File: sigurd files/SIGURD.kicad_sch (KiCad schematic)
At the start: 79 parts, among them J1 jst_sh 4, J10 CAN out (optional), J11 12V/24V Terminal, J2 Hall sensor, J3 12V Terminal, J4 PWM, J5 24V Terminal, J6 Step Up Terminal, J7 Motor Terminal, J8 INPUT, J9 CAN input, Q1 MMBT3904, U1 LMR50410Y5FQDBVRQ1, U2 STM32U575CGTx, U6 AMS1117-3.3, U8 TCAN334GDCN, Y1 48MHz

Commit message: funny fortnite
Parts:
- added D11: LED, LED_SMD:LED_0603_1608Metric_Pad1.05x0.95mm_HandSolder, symbol Device:LED
- added JP3: SolderJumper_2_Open, Jumper:SolderJumper-2_P1.3mm_Open_TrianglePad1.0x1.5mm, symbol Jumper:SolderJumper_2_Open
- added R31: 1k, Resistor_SMD:R_0603_1608Metric_Pad0.98x0.95mm_HandSolder, symbol Device:R_Small
- added R34: 120, Resistor_SMD:R_0603_1608Metric_Pad0.98x0.95mm_HandSolder, symbol Device:R_Small
- R10, R11, R12, R4, R6, R7: footprint Resistor_SMD:R_0201_0603Metric_Pad0.64x0.40mm_HandSolder -> Resistor_SMD:R_0603_1608Metric_Pad0.98x0.95mm_HandSolder
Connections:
- net +3V3: now also R31.1
- net CAN_H: now also R34.1
- net CAN_L: now also JP3.1 (A)
- net Earth: now also D11.1 (K)
- net VCC: now also J6.3 (Pin_3); no longer J6.2 (Pin_2)
- net at F2.2: now also J6.2 (Pin_2); no longer J6.3 (Pin_3)
- new net: JP3.2 (B), R34.2
- new net: D11.2 (A), R31.2
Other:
- note added: "naming"
- moved on the sheet: C1, C15, C16, C17, C18, C19, C2, C9, F1, FB1, L1, R20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

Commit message: big chungus wholesome 100
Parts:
- removed JP1: SolderJumper_2_Open, Jumper:SolderJumper-2_P1.3mm_Open_TrianglePad1.0x1.5mm, symbol Jumper:SolderJumper_2_Open
- removed R19: 120, Resistor_SMD:R_0603_1608Metric_Pad0.98x0.95mm_HandSolder, symbol Device:R_Small
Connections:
- net pull_1: now also J2.1 (Pin_1), R10.1, R35.2; no longer J2.3 (Pin_3), R37.2, R4.1
- net pull_3: now also J2.3 (Pin_3), R37.2, R4.1; no longer J2.1 (Pin_1), R10.1, R35.2
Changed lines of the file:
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@@
 	(wire
 		(pts
-			(xy 375.92 133.35) (xy 375.92 125.73)
-		)
-		(stroke
-			(width 0)
-			(type default)
-			(color 47 31 255 1)
-		)
-	)
-	(wire
-		(pts
 			(xy 120.65 165.1) (xy 125.73 165.1)
 		)
@@
 	(wire
 		(pts
-			(xy 375.92 116.84) (xy 375.92 118.11)
-		)
-		(stroke
-			(width 0)
-			(type default)
-		)
-	)
-	(wire
-		(pts
 			(xy 97.79 64.77) (xy 97.79 63.5)
 		)
@@
 	(wire
 		(pts
-			(xy 375.92 111.76) (xy 375.92 104.14)
-		)
-		(stroke
-			(width 0)
-			(type default)
-			(color 255 3 242 1)
-		)
-	)
-	(wire
-		(pts
 			(xy 116.84 251.46) (xy 116.84 248.92)
 		)
@@
 		)
 	)
-	(label "pull_1"
-		(at 46.99 119.38 270)
-		(fields_autoplaced yes)
-		(effects
-			(font
-				(size 1.27 1.27)
-			)
-			(justify right bottom)
-		)
-	)
 	(label "SOL3"
 		(at 226.06 144.78 180)
@@
 	)
 	(label "pull_3"
-		(at 74.93 106.68 270)
+		(at 55.88 106.68 270)
 		(fields_autoplaced yes)
 		(effects
@@
 		)
 	)
-	(label "pull_3"
-		(at 81.28 118.11 270)
-		(fields_autoplaced yes)
-		(effects
-			(font
-				(size 1.27 1.27)
-			)
-			(justify right bottom)
-		)
-	)
 	(label "LED_RX"
 		(at 168.91 160.02 0)
@@
 		)
 	)
-	(label "SOL2_OUT"
-		(at 331.47 179.07 180)
+	(label "pull_1"
+		(at 74.93 106.68 270)
 		(fields_autoplaced yes)
 		(effects
@@
 		)
 	)
-	(label "pull_1"
-		(at 55.88 106.68 270)
+	(label "SOL2_OUT"
+		(at 331.47 179.07 180)
 		(fields_autoplaced yes)
 		(effects
@@
 		)
 	)
+	(label "pull_1"
+		(at 81.28 118.11 270)
+		(fields_autoplaced yes)
+		(effects
+			(font
+				(size 1.27 1.27)
+			)
+			(justify right bottom)
+		)
+	)
 	(label "LED_RX"
 		(at 91.44 46.99 0)
@@
 		)
 	)
+	(label "pull_3"
+		(at 46.99 119.38 270)
+		(fields_autoplaced yes)
+		(effects
+			(font
+				(size 1.27 1.27)
+			)
+			(justify right bottom)
+		)
+	)
 	(label "HALL1_buff"
 		(at 226.06 127 180)
@@
 		)
 	)
-	(label "CAN_H"
-		(at 375.92 104.14 0)
-		(fields_autoplaced yes)
-		(effects
-			(font
-				(size 1.27 1.27)
-				(color 255 3 242 1)
-			)
-			(justify left bottom)
-		)
-	)
 	(label "SOL3_SENSE"
 		(at 330.2 200.66 180)
@@
 		)
 	)
-	(label "CAN_L"
-		(at 375.92 133.35 0)
-		(fields_autoplaced yes)
-		(effects
-			(font
-				(size 1.27 1.27)
-				(color 47 31 255 1)
-			)
-			(justify left bottom)
-		)
-	)
 	(label "SOL2"
 		(at 226.06 142.24 180)
@@
 	)
 	(symbol
-		(lib_id "Device:R_Small")
-		(at 375.92 114.3 0)
-		(unit 1)
-		(exclude_from_sim no)
-		(in_bom yes)
-		(on_board yes)
-		(dnp no)
-		(property "Reference" "R19"
-			(at 372.364 115.316 0)
-			(effects
-				(font
-					(size 1.27 1.27)
-				)
-			)
-		)
-		(property "Value" "120"
-			(at 372.364 113.284 0)
-			(effects
-				(font
-					(size 1.27 1.27)
-				)
-			)
-		)
-		(property "Footprint" "Resistor_SMD:R_0603_1608Metric_Pad0.98x0.95mm_HandSolder"
-			(at 375.92 114.3 0)
-			(effects
-				(font
-					(size 1.27 1.27)
-				)
-				(hide yes)
-			)
-		)
-		(property "Datasheet" "~"
-			(at 375.92 114.3 0)
-			(effects
-				(font
-					(size 1.27 1.27)
-				)
-				(hide yes)
-			)
-		)
-		(property "Description" ""
-			(at 375.92 114.3 0)
-			(effects
-				(font
-					(size 1.27 1.27)
-				)
-				(hide yes)
-			)
-		)
-		(pin "1"
-		)
-		(pin "2"
-		)
-		(instances
-			(project "SIGURD"
-				(path "/a4a592a3-08d1-41ec-9dda-18a75407e2f6"
-					(reference "R19")
-					(unit 1)
-				)
-			)
-		)
-	)
-	(symbol
 		(lib_id "1N4448:1N4448")
 		(at 48.26 52.07 90)
@@
 					(unit 1)
 				)
-			)
-		)
-	)
-	(symbol
-		(lib_id "Jumper:SolderJumper_2_Open")
-		(at 375.92 121.92 270)
-		(unit 1)
-		(exclude_from_sim no)
-		(in_bom yes)
-		(on_board yes)
-		(dnp no)
-		(property "Reference" "JP1"
-			(at 379.73 122.174 90)
-			(effects
-				(font
-					(size 1.27 1.27)
-				)
-			)
-		)
-		(property "Value" "SolderJumper_2_Open"
-			(at 379.73 121.92 0)
-			(effects
-				(font
-					(size 1.27 1.27)
-				)
-				(hide yes)
-			)
-		)
-		(property "Footprint" "Jumper:SolderJumper-2_P1.3mm_Open_TrianglePad1.0x1.5mm"
-			(at 375.92 121.92 0)
-			(effects
-				(font
-					(size 1.27 1.27)
-				)
-				(hide yes)
-			)
-		)
-		(property "Datasheet" "~"
-			(at 375.92 121.92 0)
-			(effects
-				(font
-					(size 1.27 1.27)
-				)
-				(hide yes)
-			)
-		)
-		(property "Description" ""
-			(at 375.92 121.92 0)
-			(effects
-				(font
-					(size 1.27 1.27)
-				)
-				(hide yes)
-			)
-		)
-		(pin "1"
-		)
-		(pin "2"
-		)
-		(instances
-			(project "SIGURD"
-				(path "/a4a592a3-08d1-41ec-9dda-18a75407e2f6"
-					(reference "JP1")
-					(unit 1)
-				)

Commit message: Goober
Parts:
- removed CR1: 1N4448, 1N4448:SOD27_NEX, symbol 1N4448:1N4448
- added D12: D, Diode_SMD:D_SOD-523, symbol Device:D
- F1: value 1.5A -> 1.0A
- R21, R23: value 470 -> ~
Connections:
- net +3V3: now also D12.1 (K)
- net V_input: now reaches F3.1, J8.2 (Pin_2)
- net at BZ1.2 (+), Q1.3 (C): now also D12.2 (A)
- net MOTOR: no longer names the net of U2.17 (PA7)
- net VCC renamed +10V
- no-connect marks 14 -> 15
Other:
- moved on the sheet: F3

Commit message: Everything but power traces routed
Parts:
- removed D9: IN-S128TATRGB, LED_SMD:LED_RGB_1210, symbol Device:LED_ARGB
- removed F1: 1.0A, Fuse:Fuse_1812_4532Metric_Pad1.30x3.40mm_HandSolder, symbol Device:Polyfuse
- removed R22: 330, Resistor_SMD:R_0603_1608Metric_Pad0.98x0.95mm_HandSolder, symbol Device:R_Small
- added D5: LED_ARBG, LED_SMD:LED_Lumex_SML-LX0404SIUPGUSB, symbol Device:LED_ARBG
- added F3: Fuse, Fuse:Fuse_1206_3216Metric, symbol Device:Fuse
- added J12: Extra NF, Connector_PinHeader_2.54mm:PinHeader_1x05_P2.54mm_Vertical, symbol Connector:Conn_01x05_Pin
- added R1: 56, LED_SMD:LED_0603_1608Metric, symbol Device:R
- added R40: 22, Resistor_SMD:R_0603_1608Metric, symbol Device:R
- added R41: 56, Resistor_SMD:R_0603_1608Metric, symbol Device:R
- F1: renamed from F3; footprint Fuse:Fuse_1812_4532Metric_Pad1.30x3.40mm_HandSolder -> Fuse:Fuse_1206_3216Metric
- F2: value 4A -> 5A; footprint Fuse:Fuse_1812_4532Metric_Pad1.30x3.40mm_HandSolder -> Fuse:Fuse_1206_3216Metric
- U4: renamed from U1; footprint DBV0006A-IPC_A -> (none)
- renumbered C10 to C1, C11 to C10, C6 to C11, C1 to C12, C2 to C13, C9 to C14, C17 to C16, C18 to C17, C19 to C18, C16 to C19, C12 to C2, C13 to C3, C14 to C4, C4 to C5, C5 to C6, C8 to C7, C20 to C8, C7 to C9, CR2 to CR1, CR3 to CR2, D2 to D1, D12 to D2, D13 to D3, D14 to D4, D8 to D6, D11 to D7, J8 to J1, J5 to J10, J9 to J2, J10 to J3, J1 to J4, J6 to J5, J4 to J6, J2 to J8, J3 to J9, JP3 to JP1, R34 to R10, R5 to R11, R9 to R12, R16 to R13, R17 to R14, R18 to R15, R4 to R16, R7 to R17, R10 to R18, R6 to R19, R11 to R20, R12 to R21, R31 to R22, R3 to R23, R20 to R24, R1 to R3, R21 to R4, R23 to R5, R37 to R6, R36 to R7, R35 to R8, R8 to R9, U8 to U1, U6 to U3
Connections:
- net +10V: now also F3.1
- net +24V: now also J5.2 (Pin_2); no longer J7.1 (Pin_1)
- net +3V3: now also D5.1 (A)
- net LED_B: now also U2.11 (PA1), R41.1; no longer U2.12 (PA2)
- net LED_G: now also U2.12 (PA2), R40.1; no longer U2.11 (PA1)
- net LED_R: now also R1.1
- net at C12.2, FB1.2: now also F3.2
- net PA7: now reaches U2.17 (PA7)
- net PA7: now also J12.1 (Pin_1)
- net PB0: now reaches U2.18 (PB0)
- net PB0: now also J12.2 (Pin_2)
- net PB1: now reaches U2.19 (PB1)
- net PB1: now also J12.3 (Pin_3)
- net PB2: now reaches U2.20 (PB2)
- net PB2: now also J12.4 (Pin_4)
- net PB10: now reaches U2.21 (PB10)
- net PB10: now also J12.5 (Pin_5)
- net at F2.2: now also J7.1 (Pin_1); no longer J5.2 (Pin_2)
- new net: D5.3 (BK), R41.2
- new net: D5.2 (RK), R1.2
- new net: D5.4 (GK), R40.2
- no-connect marks 15 -> 10
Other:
- moved on the sheet: F2, J7

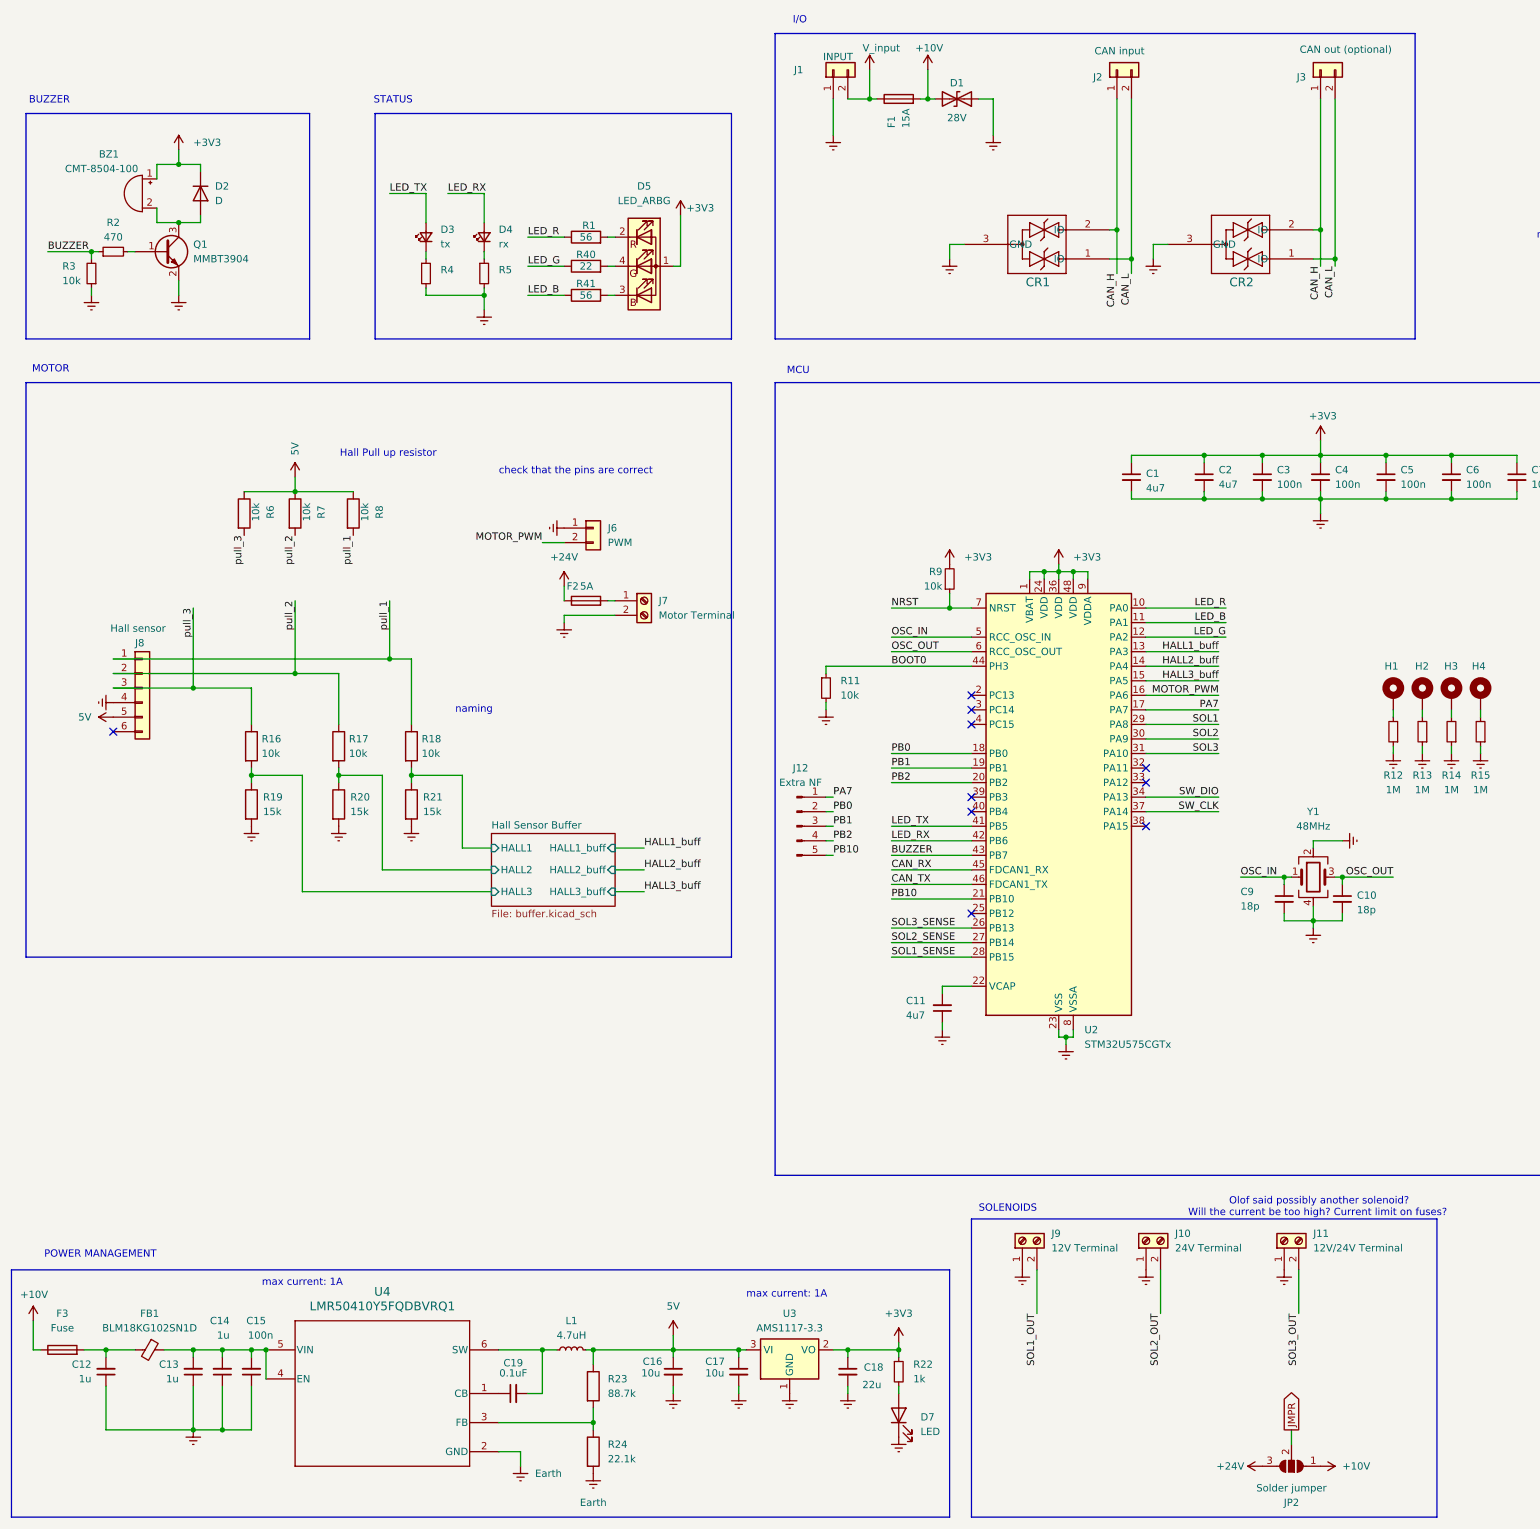
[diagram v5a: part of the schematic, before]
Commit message: fixed pcb errors and most warnings
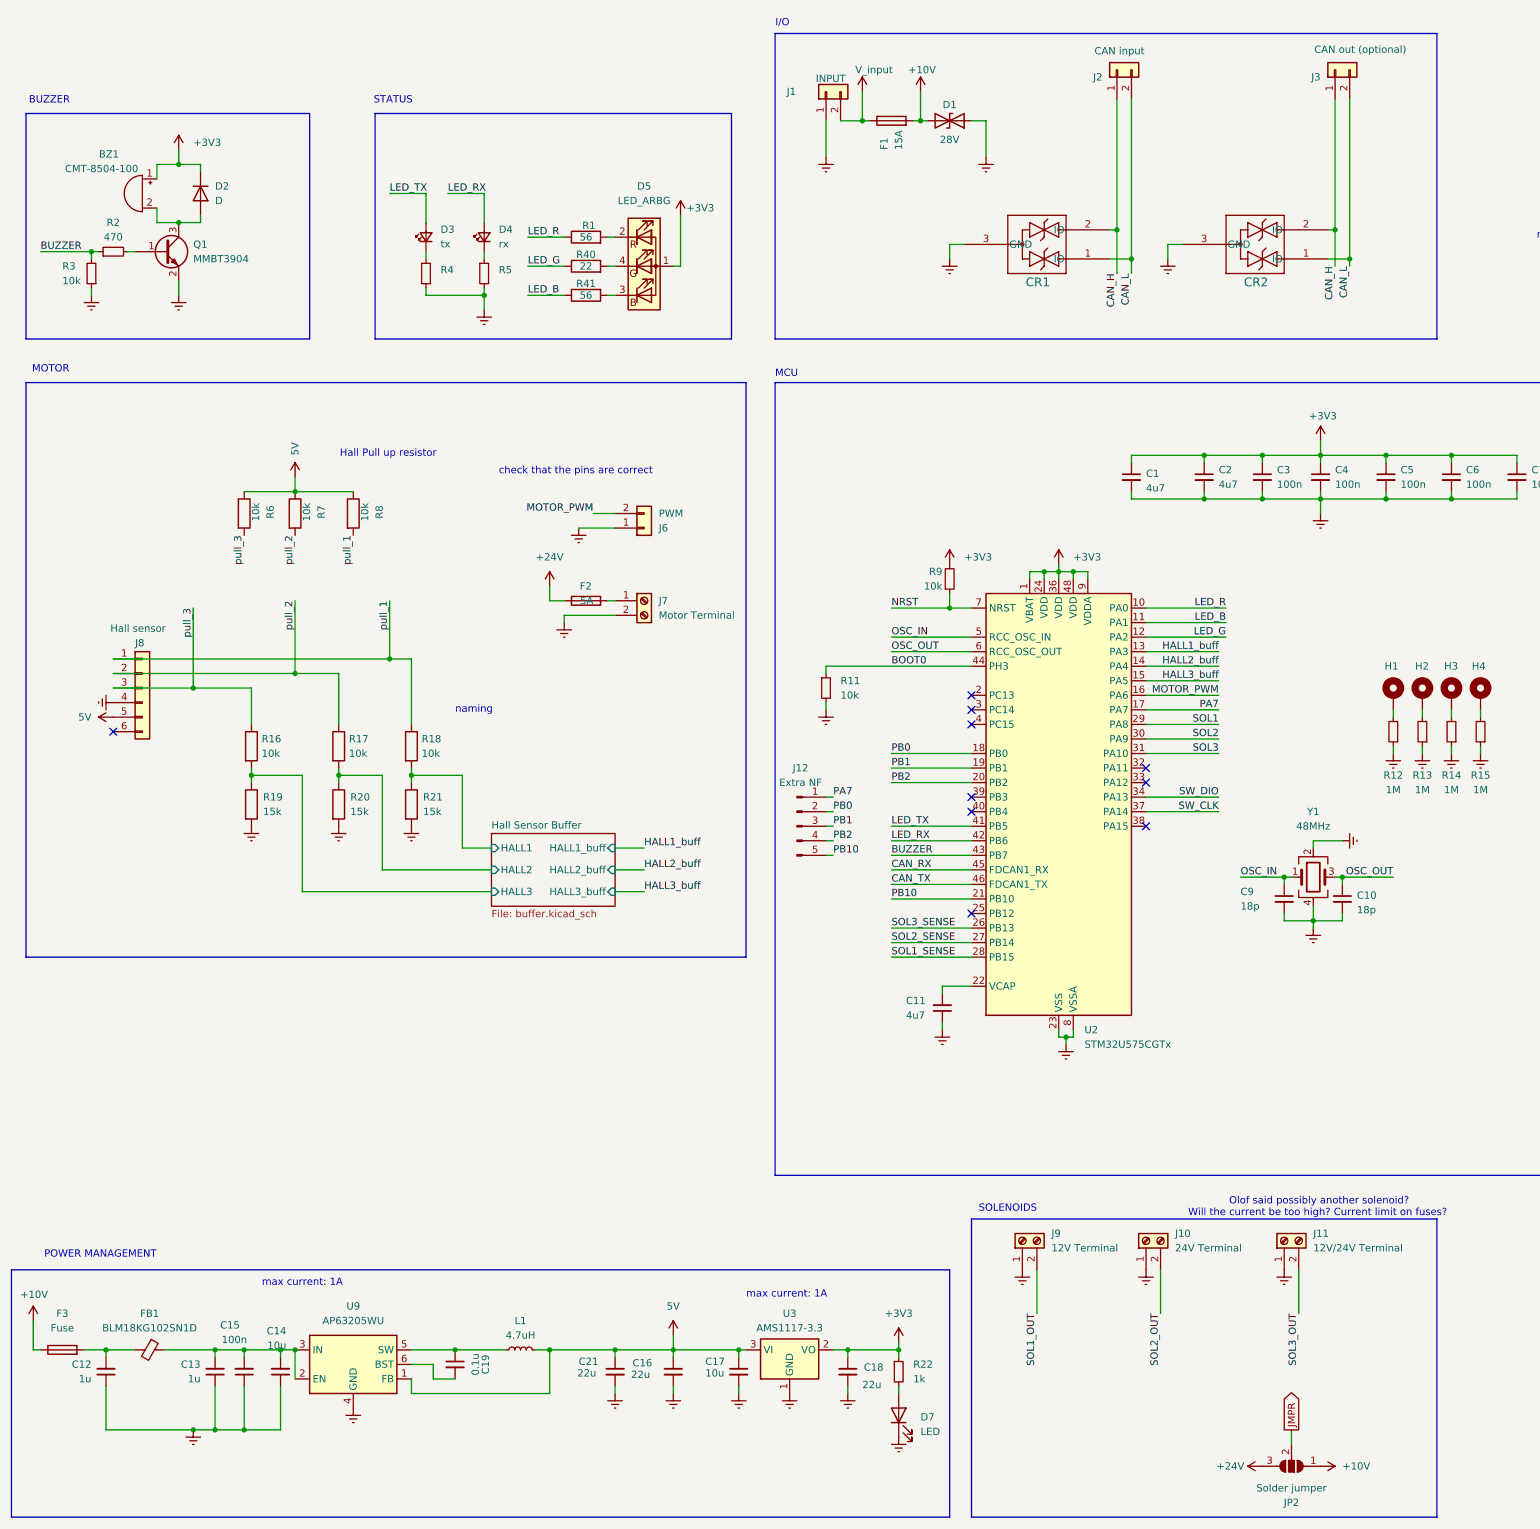
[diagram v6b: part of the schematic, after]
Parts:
- removed R23: 88.7k, Resistor_SMD:R_0603_1608Metric_Pad0.98x0.95mm_HandSolder, symbol Device:R
- removed R24: 22.1k, Resistor_SMD:R_0603_1608Metric_Pad0.98x0.95mm_HandSolder, symbol Device:R
- removed U4: LMR50410Y5FQDBVRQ1, symbol LMR50410Y5FQDBVRQ1:LMR50410Y5FQDBVRQ1
- added C21: 22u, Capacitor_SMD:C_0603_1608Metric_Pad1.08x0.95mm_HandSolder, symbol Device:C_Small
- added U9: AP63205WU, Package_TO_SOT_SMD:TSOT-23-6, symbol Regulator_Switching:AP63205WU
- C14: value 1u -> 10u
- C16: value 10u -> 22u
- C19: value 0.1uF -> 0.1u
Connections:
- net 5V: now also C21.1, U9.1 (FB)
- net Earth: now also C21.2, U9.4 (GND)
- net at C19.1: now also L1.1, U9.5 (SW)
- net at C19.2: now also U9.6 (BST); no longer L1.1
- net at C13.2, C14.2, C15.2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: now also U9.2 (EN), U9.3 (IN)
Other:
- moved on the sheet: C13, C14, C15, C19, CR2, D1, F1, J1, J3, J6, L1
